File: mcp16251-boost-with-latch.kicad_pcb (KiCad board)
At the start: 2 copper layers, 33 x 22.9 mm, 30 parts, among them J1 THT_Castellated, J10 THT_Castellated, J11 SMD_pad, J2 THT_Castellated, J3 THT_Castellated, J4 SMD_pad, J5 SMD_pad, J6 SMD_pad, J7 SMD_pad, J8 SMD_pad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

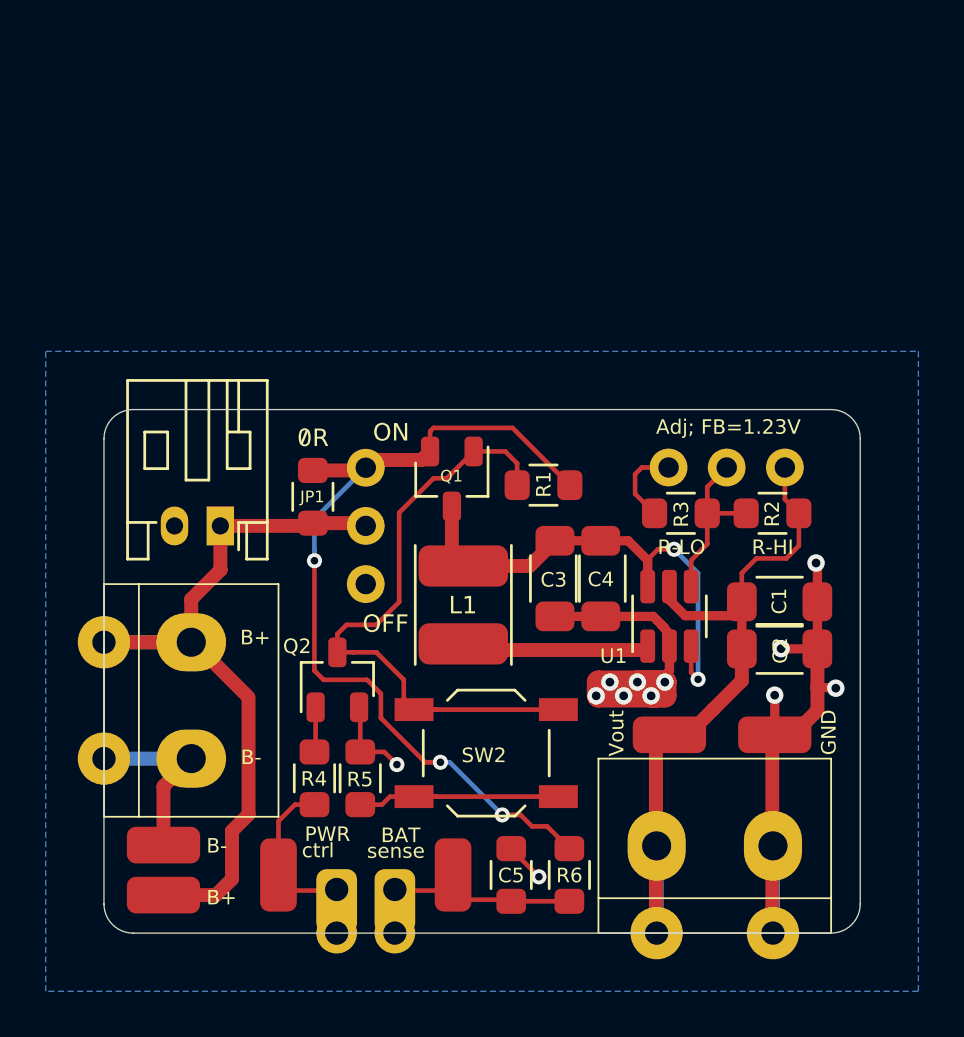
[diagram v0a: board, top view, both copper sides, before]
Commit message: Schematic tuning, footprint assignment, netlist.
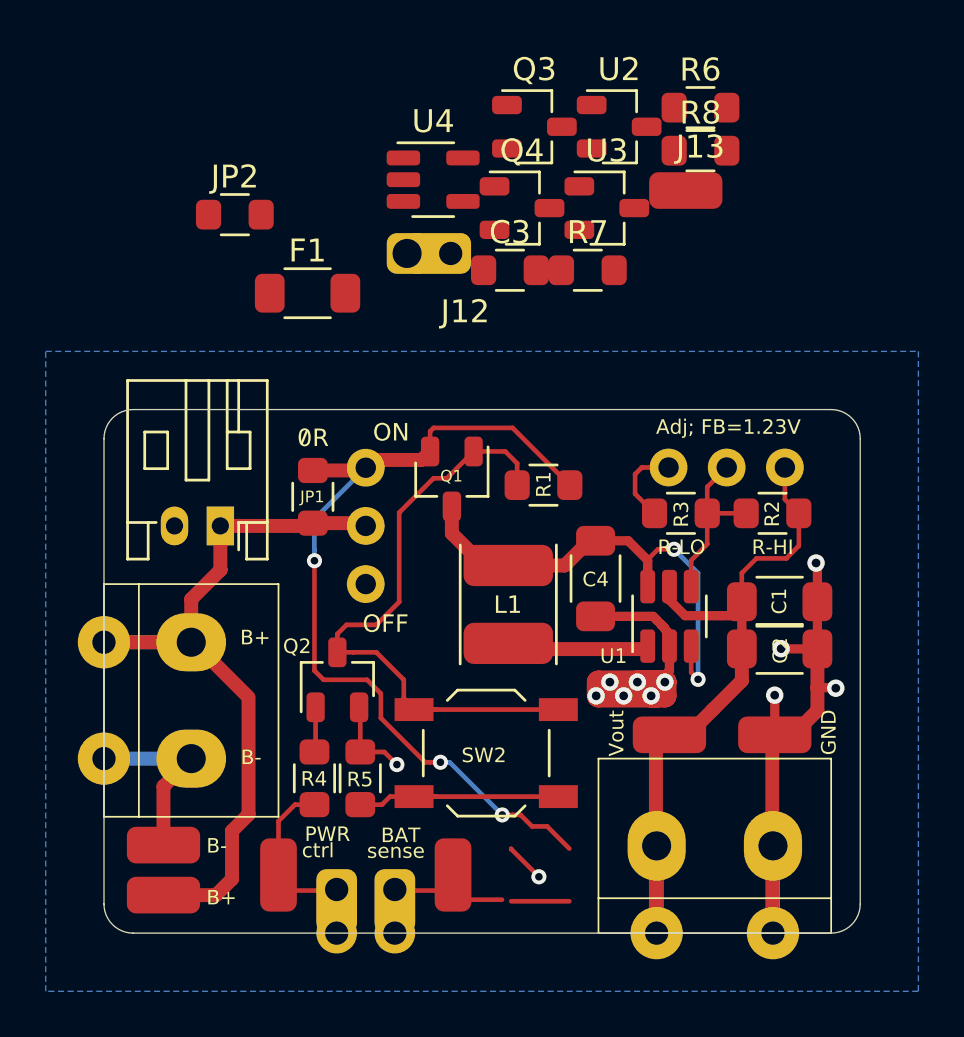
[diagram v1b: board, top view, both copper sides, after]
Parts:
- removed C5: 100nF, MCP16251_module:R_0805_HS
- added F1: Polyfuse, MCP16251_module:R_1206_HS, F.Cu at (139.7, 71.1)
- added J12: THT_Castellated, MCP16251_module:Conn_01x01_cast, F.Cu at (144.0, 69.4)
- added J13: SMD_pad, MCP16251_module:SMD-Pad_01x01, F.Cu at (156.2, 66.6)
- added JP2: Jumper, MCP16251_module:R_0805_HS, F.Cu at (136.5, 67.7)
- added Q3: Q_PMOS_GSD, MCP16251_module:SOT-23_HS, F.Cu at (149.6, 63.9)
- added Q4: Q_PMOS_GSD, MCP16251_module:SOT-23_HS, F.Cu at (149.1, 67.4)
- added R7: 1k, MCP16251_module:R_0805_HS, F.Cu at (151.9, 70.1)
- added R8: 100k, MCP16251_module:R_0805_HS, F.Cu at (156.9, 64.9)
- added U2: MIC809, MCP16251_module:SOT-23_HS, F.Cu at (153.3, 63.9)
- added U3: MIC803, MCP16251_module:SOT-23_HS, F.Cu at (152.8, 67.4)
- added U4: MIC2777, MCP16251_module:SOT-23-5_HS, F.Cu at (145.2, 66.2)
- C3: value CP1 -> 100nF; footprint MCP16251_module:R_1206_HS -> MCP16251_module:R_0805_HS
- R5, R6: value 1k -> 100k
- moved R6 34.0 mm to (156.9, 63.0), turned to 0 degrees
- moved C3 13.6 mm to (148.5, 70.1), turned to 0 degrees
- moved L1 1.96 mm to (148.5, 84.7)
- moved C4 0.23 mm to (152.3, 83.6)
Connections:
- net VCC renamed 5V
- C3 pad 1: VBAT -> uC_ADC
- J3 pad 1: Net-(C5-Pad1) -> uC_ADC
- J4 pad 1: Net-(C5-Pad1) -> uC_ADC
- JP1 pad 1: VBAT_RAW -> Net-(F1-Pad1)
- R5 pad 1: Net-(R5-Pad1) -> PWR_CONTROL
- R6 pad 1: Net-(C5-Pad1) -> BOOST_EN
- R6 pad 2: Vbat_raw_sense -> GND
- SW1 pad 2: VBAT_RAW -> Net-(F1-Pad1)
- SW2 pad 1: Net-(R5-Pad1) -> GND
- U1 pad 3: VBAT -> BOOST_EN
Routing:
- net uC_ADC: track 0.00 -> 6.74 mm
- net Net-(C5-Pad1): track 9.28 -> 2.54 mm
- net GND: track 57.2 -> 55.2 mm
- net Net-(L1-Pad2): track 8.09 -> 6.14 mm
- net VBAT: track 22.0 -> 21.3 mm
